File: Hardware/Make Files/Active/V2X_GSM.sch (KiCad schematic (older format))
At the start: 35 parts, among them P6 SMA, P7 SMA, P8 47553-1001, Q12 2N3904, Q13 2N3904, U16 SIM5320, U17 SMF05

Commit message: Saving V1.1 as archive.
We are trying a new architecture where the FTDI can be removed. making a
backup spot
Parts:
- removed C44: 10N, Capacitors_SMD:C_0603, symbol C
- removed C49: 50P, Capacitors_SMD:C_0603, symbol C
- removed C51: 100N, Capacitors_SMD:C_0603, symbol C
- removed C52: 330P, Capacitors_SMD:C_0603, symbol C
- removed D10: BLUE, LEDs:LED-0805, symbol LED
- removed D11: RED, LEDs:LED-0805, symbol LED
- removed L3: 47N, Capacitors_SMD:C_0805, symbol INDUCTOR_SMALL
- removed P6: SMA, Custom Parts:SMA-RA_142-0701-801, symbol CONN_01X02
- removed Q12, Q13: 2N3904, Housings_SOT-23_SOT-143_TSOT-6:SOT-23, symbol Q_NPN_BEC
- removed R64, R65: 22, Resistors_SMD:R_0603, symbol R
- removed R66, R67: 330, Resistors_SMD:R_0603, symbol R
- removed R68: 2K2, Resistors_SMD:R_0603, symbol R
- removed R69: 2.2K, Resistors_SMD:R_0603, symbol R
- removed R70, R71: 10K, Resistors_SMD:R_0603, symbol R
- removed R73: dns, Resistors_SMD:R_0603, symbol R
- added C16, C27: 100N, Capacitors_SMD:C_0603, symbol C
- added C17: 330P, Capacitors_SMD:C_0603, symbol C
- added C20, C28: 10N, Capacitors_SMD:C_0603, symbol C
- added C24: 50P, Capacitors_SMD:C_0603, symbol C
- added C25: 220U, Capacitors_SMD:C_0603, symbol CP
- added C26, C29: 4U7, Capacitors_SMD:C_0603, symbol C
- added FB3: 220, Capacitors_SMD:C_0805, symbol FILTER
- added L2: 47N, Capacitors_SMD:C_0805, symbol INDUCTOR_SMALL
- added P2: SMA, Custom Parts:SMA-RA_142-0701-801, symbol CONN_01X02
- added R10, R9: 22, Resistors_SMD:R_0603, symbol R
- added R7, R?: DNS, Resistors_SMD:R_0603, symbol R
- added R?: 0, Resistors_SMD:R_0603, symbol R
- A1: renamed from A?; Mouse PN (none) -> 609-1575AT43A0040E
- A2: renamed from A?; Mouse PN (none) -> 673-W3544A
- C18: renamed from C42; Mouser PN (none) -> 504-KR-5R5C104-R
- C19: renamed from C43; Mouse PN (none) -> 77-VJ0603A331FXXCB
- C23: renamed from C47; Mouse PN (none) -> 80-C0603C470J5G
- L1: Mouse PN (none) -> 81-LQG18HN47NJ00D
- P1: renamed from P8; Mouse PN (none) -> 538-47553-1001
- P3: renamed from P7; Mouse PN (none) -> 530-142-0701-801
- R6: renamed from R72; value 4K7 -> DNS
- R8: renamed from R63; Mouse PN (none) -> 71-CRCW0603-22.1-E3
- U3: renamed from U17; Mouse PN (none) -> 863-SMF05CT1G
- U4: renamed from U16; AliExpress PN (none) -> SIM5320A; Mouse PN (none) -> #
- W1: Mouse PN (none) -> 523-192113
- W2: Mouse PN (none) -> 815-APAMPS-105
- gave numbers to parts that had none: 2
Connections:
- net labels added: HUB_PWR_PRT2, PC_WAKE, SIM_DM, SIM_DP, SIM_DTR, SIM_NET, SIM_PWR, SIM_PWR_ON, SIM_RF_OFF, SIM_RI, SIM_RXD, SIM_TXD, SIM_VBUS, SIM_WAKE
- net labels removed: 3V3, ADC1, ADC2, EAR_N, EAR_P, GPIO_1, GPIO_4, GPIO_40, GPIO_41, GPIO_42, GPIO_43, GPIO_44, GPRS_EN, GPRS_RESET, GSM_DM, GSM_DP, GSM_VBUS, I2C_SCL, I2C_SDA, KEY_N0, KEY_N1, KEY_N2, KEY_N3, KEY_N4, KEY_P0, KEY_P1, KEY_P2, KEY_P3, KEY_P4, MIC_N, MIC_P, PCM_CLK, PCM_DIN, PCM_DOUT, PCM_SYNC, SPI_CLK, SPI_CS, SPI_MISO, SPI_MOSI, SPK_N, SPK_P, UART_CTS, UART_DCD, UART_DTR, UART_RI, UART_RTS, UART_RXD, UART_TXD
- wire segments 49 -> 47
- no-connect marks 7 -> 40
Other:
- note added: "Hopefully the PWRCTRL can \nmomentarily use a pull up \nresistor to snense the card,\n otherwise resistors"
- note removed: "Network Status LED"
- note removed: "Power Status LED"
- moved on the sheet: P1, R6

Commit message: V1.2 mostly done
BOM is integrated and creates mouser orders
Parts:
- removed U3: SMF05, Housings_SOT-23_SOT-143_TSOT-6:SC-70-6_Handsoldering, symbol SMF05
- added C28: 220U, Capacitors_SMD:C_0603, symbol CP
- added U?: MMQA5V6T3G, symbol ESDAxxSC6
- R11: renamed from R?; Mouse PN 71-CRCW0603-22.1-E3 -> 71-CRCW0603-0-E3
- gave numbers to parts that had none: 1
- renumbered C28 to C29, C29 to C30, R8 to R12, R9 to R13, R10 to R14, R6 to R8, R7 to R9
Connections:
- net labels added: SIMCARD_CLK, SIMCARD_DATA, SIMCARD_RESET, SIMCARD_V
- net labels removed: SIM_CLK, SIM_DATA, SIM_V
- wire segments 47 -> 49
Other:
- moved on the sheet: C16, C17, C29, C30, L2

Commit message: V2X v1.2 sch and bom
Made changes to the schematic to V1.2 (remove FTDI possibly) and
integrade the BOM information into the sch
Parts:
- FB3: Mouse PN 81-BLM21P221SG -> 810-MPZ1608S221ATA00
- gave numbers to parts that had none: 1
- renumbered C16 to C14, C17 to C15, C18 to C16, C19 to C17, C20 to C18, C21 to C19, C22 to C20, C23 to C21, C24 to C22, C25 to C23, C26 to C24, C27 to C25, C28 to C26, C29 to C27, C30 to C28

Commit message: Split V2X in 2 boards, layout of SIM pcb done
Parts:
- removed A1, A2: ANTENNEA, symbol ANTENNEA
- removed W1: FME<->SMA, symbol TEST
- added L6, L7: 47N, Custom Parts:C_0603_SM, symbol INDUCTOR_SMALL
- added P25, P26: CONN_02X08, Pin_Headers:Pin_Header_Straight_2x10, symbol CONN_02X10
- added R84, R86: DNS, Custom Parts:R_0603_sm, symbol R
- added R85: 0, Custom Parts:R_0603_sm, symbol R
- C14, C15, C17, C18, C25, C27: footprint Capacitors_SMD:C_0603 -> Custom Parts:C_0603_SM
- C19: value DNS -> 330P; footprint Capacitors_SMD:C_0603 -> Custom Parts:C_0603_SM; Mouse PN (none) -> 77-VJ0603A331FXXCB
- C20: value DNS -> 10N; footprint Capacitors_SMD:C_0603 -> Custom Parts:C_0603_SM; Mouse PN (none) -> 77-VJ0603Y103KXACBC
- C21, C22: value 50P -> 47p; footprint Capacitors_SMD:C_0603 -> Custom Parts:C_0603_SM; Mouse PN 80-C0603C470J5G -> (none)
- C23, C26: footprint Capacitors_SMD:C_0603 -> Capacitors_SMD:c_elec_6.3x5.8
- C24, C28: footprint Capacitors_SMD:C_0603 -> Custom Parts:C_0805_SM
- FB3: footprint Capacitors_SMD:C_0805 -> Custom Parts:R_0603_sm
- L1, L2: footprint Capacitors_SMD:C_0805 -> Custom Parts:C_0603_SM
- P1: footprint Custom Parts:FSM006-2610 -> Custom Parts:47553-1001
- R10, R11, R12, R13, R14, R8, R9: footprint Resistors_SMD:R_0603 -> Custom Parts:R_0603_sm
- U3: footprint (none) -> Housings_SOT-23_SOT-143_TSOT-6:SOT-23-6
- U4: symbol SIM5320 -> SIM5320-RESCUE-V2X
- W2: Mouse PN 815-APAMPS-105 -> 815-APAMPS-106
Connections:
- net labels added: 12V0_B, 12V0_C, 4V1_A, 4V1_B, 4V1_EN, 4V1_EN_B, SEQ_WAKE, SIMCARD_B, SIM_DM_B, SIM_DP_B, SIM_NET_B, SIM_PWR_B, SIM_PWR_ON_B, SIM_RESET_B, SIM_RF_OFF_B, SIM_RXD_B, SIM_TXD_B, SIM_USB_DET, SIM_USB_DET_B
- net labels removed: 4V1
- wire segments 49 -> 56
- no-connect marks 40 -> 38
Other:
- note added: "SEQ side"
- note added: "SIM side"
- moved on the sheet: C17, C18, C23, C24, C25, C26, C27, C28, FB3, L1, L2, R10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

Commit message: V1.2 pass complete and ready to order
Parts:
- C23, C26: Size D6.3x5.8mm -> (none)
- U4: Mouse PN # -> (none)
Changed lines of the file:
@@
 F 2 "Custom Parts:SIM5320" H 2800 4100 60  0001 C CNN
 F 3 "http://www.simcom.ee/modules/wcdma-hspa/sim5320/" H 2800 4100 60  0001 C CNN
-F 4 "#" H 4150 3300 60  0001 C CNN "Mouse PN"
-F 5 "SIM5320A" H 4150 3300 60  0001 C CNN "AliExpress PN"
+F 4 "SIM5320A" H 4150 3300 60  0001 C CNN "AliExpress PN"
 	1    4150 3300
 	1    0    0    -1
@@
 F 3 "http://www.mouser.com/ds/2/445/875105244013-540575.pdf" H 2850 7400 60  0001 C CNN
 F 4 "710-875105244013" H 2850 7400 60  0001 C CNN "Mouse PN"
-F 5 "D6.3x5.8mm" H 2850 7400 60  0001 C CNN "Size"
 	1    2850 7400
 	-1   0    0    -1
@@
 F 3 "http://www.mouser.com/ds/2/445/875105244013-540575.pdf" H 4400 7400 60  0001 C CNN
 F 4 "710-875105244013" H 4400 7400 60  0001 C CNN "Mouse PN"
-F 5 "D6.3x5.8mm" H 4400 7400 60  0001 C CNN "Size"
 	1    4400 7400
 	-1   0    0    -1

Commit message: Project rework
Split the Main and GSM boards into separate projects, redesigned Main
board after flaws were found.
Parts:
- removed P25: CONN_02X08, Pin_Headers:Pin_Header_Straight_2x10, symbol CONN_02X10
- removed R10: DNS, Custom Parts:R_0603_sm, symbol R
- removed R11: 0, Custom Parts:R_0603_sm, symbol R
- added C?: 330P, Custom Parts:C_0603_SM, symbol C
- added C?: 4U7, Custom Parts:C_0805_SM, symbol C
- added C? (x2): 10U, Custom Parts:C_1206_SM, symbol C
- added D?: SBR3U30P1-7, Diodes_SMD:SOD-123, symbol D_Schottky_Small
- added L?: 5U6, Custom Parts:4.5x4.5mm_Ind, symbol INDUCTOR_SMALL
- added P?: CUR_SEN, Connect:PINHEAD1-2, symbol CONN_01X02
- added Q?: IRF9335, Custom Parts:SOIC-8_MOS, symbol Q_PMOS_GSD
- added R?: 2K0, Custom Parts:R_0603_sm, symbol R
- added R?: 8K2, Custom Parts:R_0603_sm, symbol R
- added U?: XRP6124, Housings_SOT-23_SOT-143_TSOT-6:SOT-23-5, symbol XRP6124
- U4: symbol SIM5320-RESCUE-V2X -> SIM5320; Mouse PN (none) -> #
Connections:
- net labels removed: 12V0_B, 4V1_A, 4V1_EN, HUB_PWR_PRT2, SEQ_WAKE, SIMCARD, SIM_DM, SIM_DP, SIM_NET, SIM_PWR, SIM_PWR_ON, SIM_RESET, SIM_RF_OFF, SIM_RXD, SIM_TXD, SIM_USB_DET, SIM_VBUS
- wire segments 56 -> 65
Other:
- note added: "4.1V @ 1.5A DC-DC Power Supply"
- note removed: "SEQ side"
- moved on the sheet: C16, C23, C24, C25, C26, C27, C28, FB3, P26, R12, R13, R14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

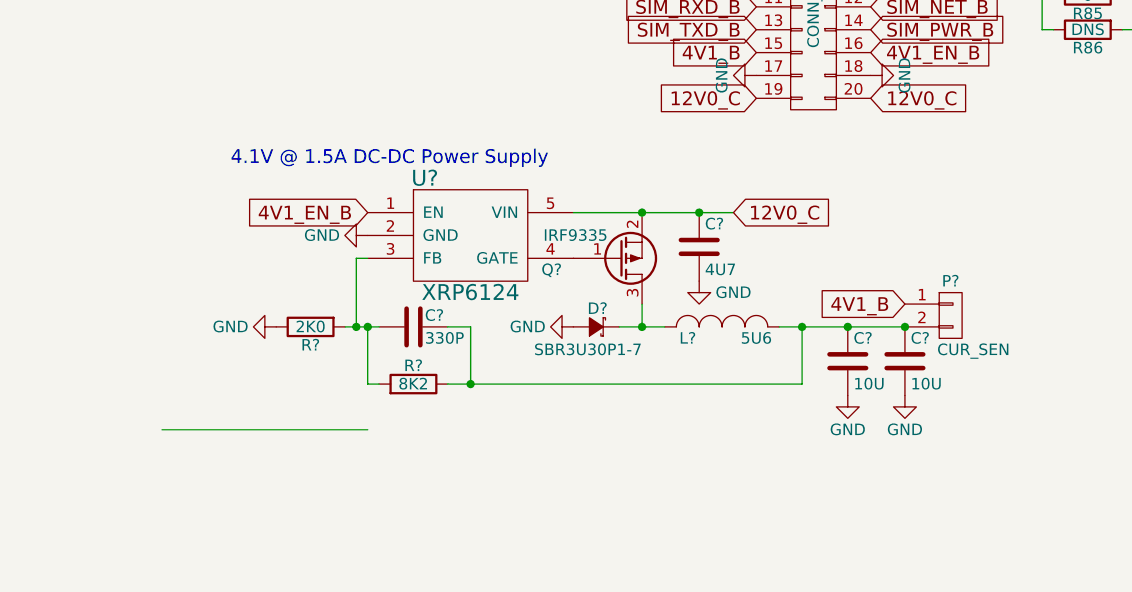
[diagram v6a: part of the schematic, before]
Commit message: Added USB-A to design
discovered the Rpi cannot be back fed over USB, had to add a power Port
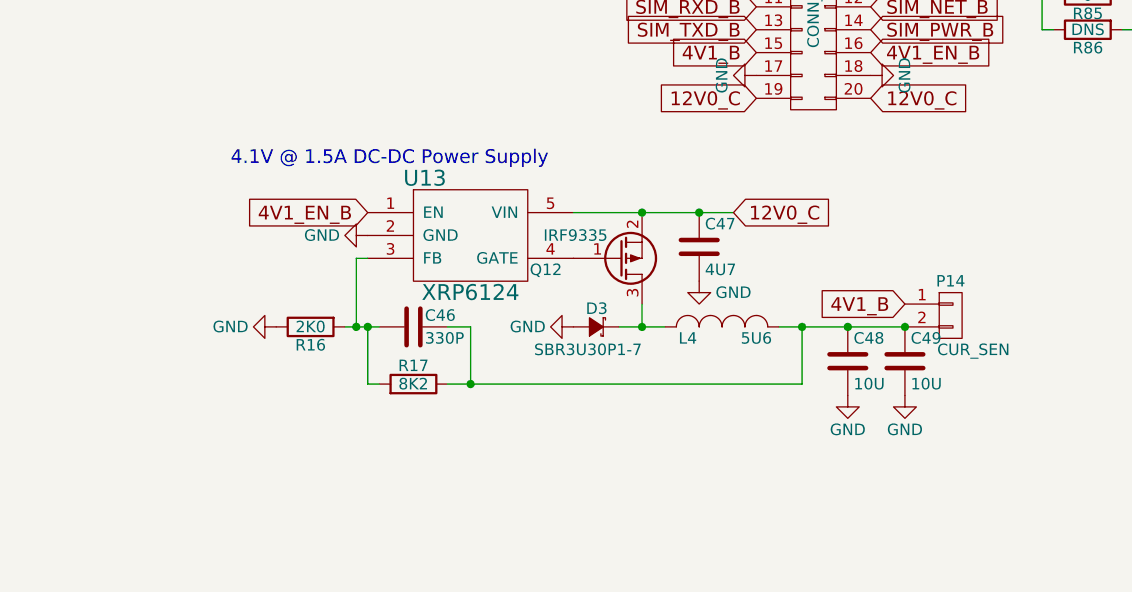
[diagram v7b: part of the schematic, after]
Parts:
- gave numbers to parts that had none: 11
